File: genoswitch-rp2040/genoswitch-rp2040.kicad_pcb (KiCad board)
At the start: 2 copper layers, 43.4 x 57.3 mm, 42 parts, among them J1 USB_B_Micro, J10 RP2040_ADC2, J11 RP2040_ADC3, J2 Conn_01x03_Socket-PicoDebug, J3 HW-SPI0, J4 HW-SPI1, J5 PIO-SPI0, J6 PIO-SPI1, J7 SERIAL, J8 RP2040_ADC0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

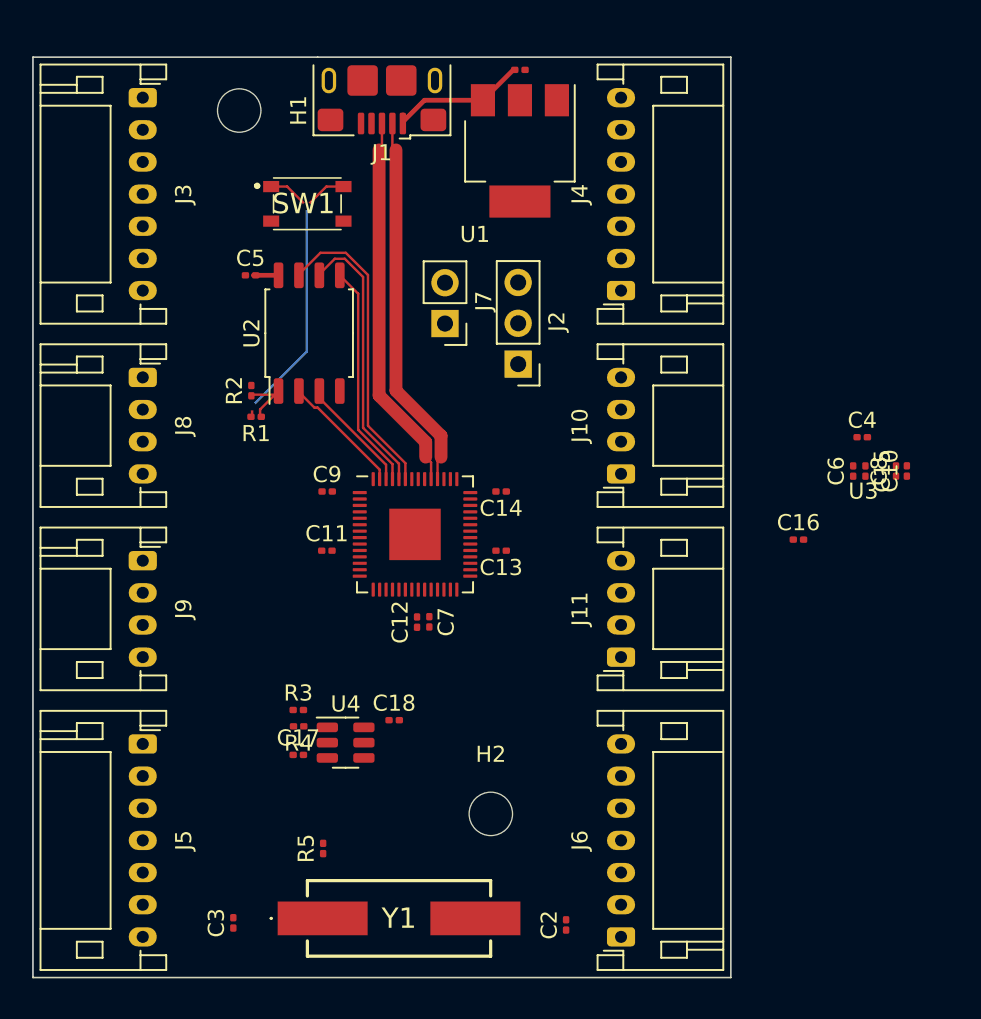
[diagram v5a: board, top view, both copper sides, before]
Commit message: Initial routing of C6, C15, C16, R6, R7
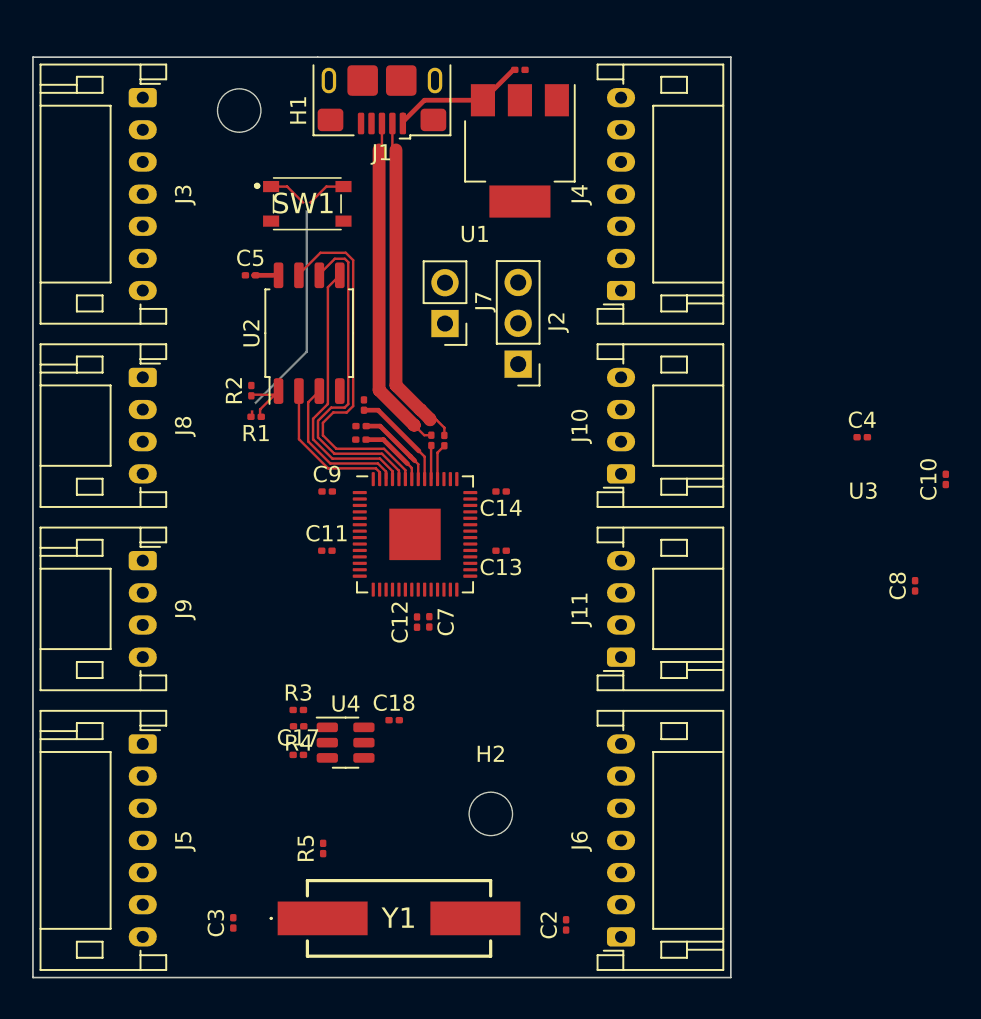
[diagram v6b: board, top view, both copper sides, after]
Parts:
- added R6: 27.4, Resistor_SMD:R_0201_0603Metric, F.Cu at (110.4, 68.1)
- added R7: 27.4, Resistor_SMD:R_0201_0603Metric, F.Cu at (111.2, 68.1)
- moved C15 31.5 mm to (106.0, 67.2), turned to 0 degrees
- moved C6 30.7 mm to (106.0, 68.0), turned to 180 degrees
- moved C16 28.3 mm to (106.2, 65.9), turned to -90 degrees
- moved C8 7.24 mm to (140.5, 77.1)
- moved C10 2.48 mm to (142.4, 70.5)
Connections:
- U3 pad 46: /USB_D- -> Net-(U3-USB_DM)
- U3 pad 47: /USB_D+ -> Net-(U3-USB_DP)
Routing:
- net GND: track 0.00 -> 11.5 mm
- net +1V1: track 0.00 -> 4.27 mm
- net /QSPI_SD3: track 19.1 -> 22.9 mm
- net /QSPI_SCLK: track 17.1 -> 20.9 mm
- net /QSPI_SD0: track 14.1 -> 17.2 mm
- net /USB_D-: track 23.5 -> 21.0 mm
- net /USB_D+: track 23.5 -> 21.1 mm
- net /QSPI_SD2: track 7.20 -> 9.51 mm
- net Net-(U3-USB_DM): track 0.00 -> 2.25 mm
- net Net-(U3-USB_DP): track 0.00 -> 2.10 mm
- net /QSPI_SD1: track 7.67 -> 9.30 mm

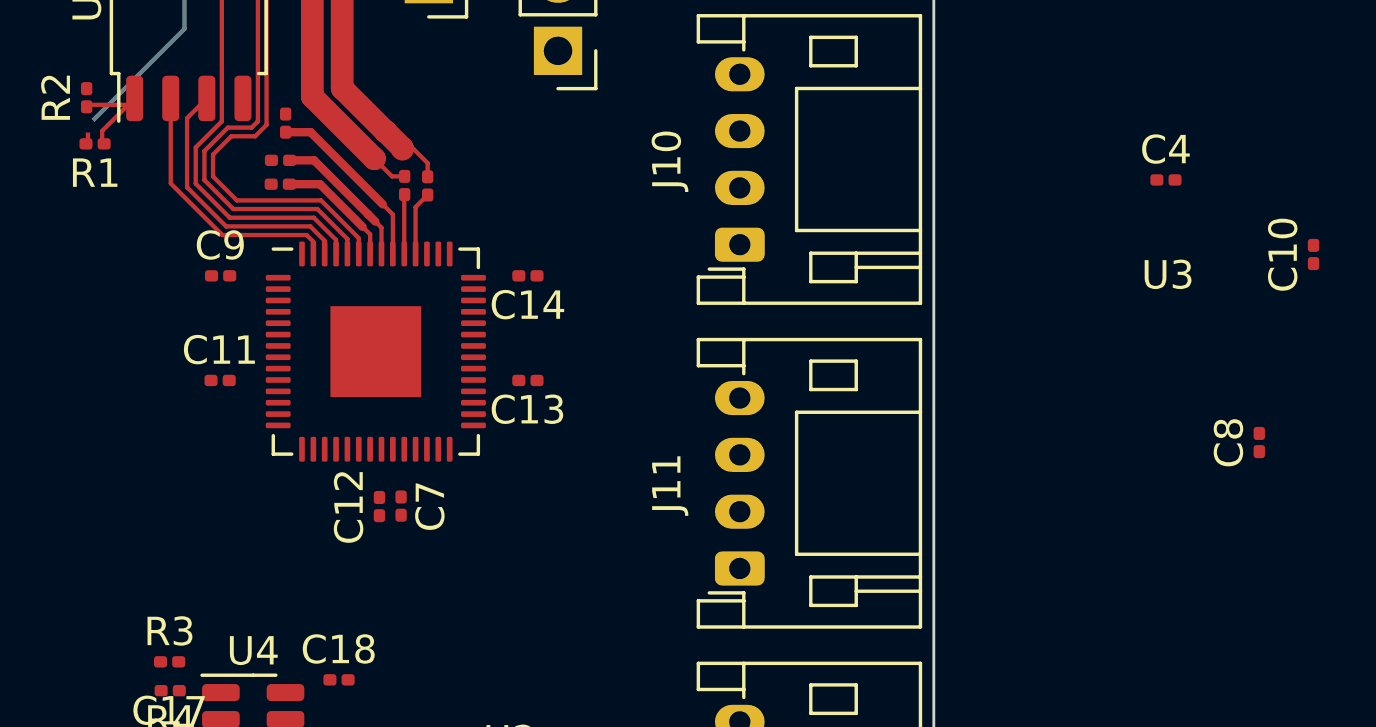
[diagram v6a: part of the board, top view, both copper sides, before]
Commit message: Route other resistors, caps on RP2040
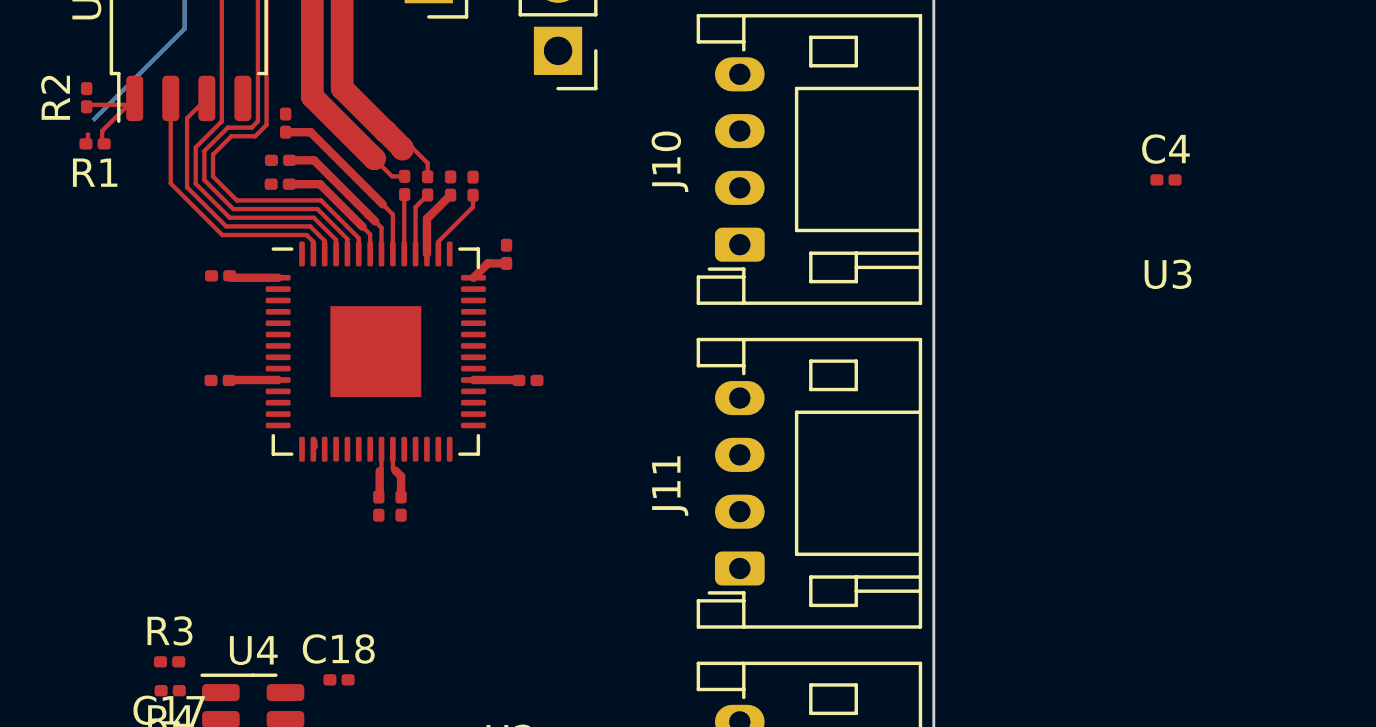
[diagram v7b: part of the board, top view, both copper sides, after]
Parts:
- moved C8 29.9 mm to (112.0, 68.1)
- moved C10 29.7 mm to (112.8, 68.1)
- moved C14 1.07 mm to (114.0, 70.5), turned to -90 degrees
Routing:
- net GND: track 11.5 -> 19.7 mm
- net +1V1: track 4.27 -> 8.49 mm
- net Net-(U3-VREG_IN): track 0.00 -> 2.58 mm
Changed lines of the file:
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@@
   (setup
     (pad_to_mask_clearance 0)
-    (grid_origin 108.712 0)
     (pcbplotparams
       (layerselection 0x00010fc_ffffffff)
@@
   )
   (footprint "Capacitor_SMD:C_0201_0603Metric" (layer "F.Cu")
-    (at 142.362 70.495 90)
+    (at 112.77 68.09 90)
     (descr "Capacitor SMD 0201 (0603 Metric), square (rectangular) end terminal, IPC_7351 nominal, (Body size source: https://www.vishay.com/docs/20052/crcw0201e3.pdf), generated with kicad-footprint-generator")
     (tags "capacitor")
@@
     (property "ki_keywords" "cap capacitor")
     (attr smd)
-    (fp_text reference "C10" (at 0 -1.05 90) (layer "F.SilkS")
+    (fp_text reference "C10" (at 0 -1.05 90) (layer "F.SilkS") hide
         (effects (font (size 1 1) (thickness 0.15)))
     )
@@
   )
   (footprint "Capacitor_SMD:C_0201_0603Metric" (layer "F.Cu")
-    (at 114.702 71.247 180)
+    (at 113.95 70.49 -90)
     (descr "Capacitor SMD 0201 (0603 Metric), square (rectangular) end terminal, IPC_7351 nominal, (Body size source: https://www.vishay.com/docs/20052/crcw0201e3.pdf), generated with kicad-footprint-generator")
     (tags "capacitor")
@@
     (property "ki_keywords" "cap capacitor")
     (attr smd)
-    (fp_text reference "C14" (at 0 -1.05 180) (layer "F.SilkS")
+    (fp_text reference "C14" (at 0 -1.05 90) (layer "F.SilkS") hide
         (effects (font (size 1 1) (thickness 0.15)))
     )
-    (fp_text value "100nF" (at 0 1.05 180) (layer "F.Fab")
+    (fp_text value "100nF" (at 0 1.05 90) (layer "F.Fab")
         (effects (font (size 1 1) (thickness 0.15)))
     )
-    (fp_text user "${REFERENCE}" (at 0 -0.68 180) (layer "F.Fab")
+    (fp_text user "${REFERENCE}" (at 0 -0.68 90) (layer "F.Fab")
         (effects (font (size 0.25 0.25) (thickness 0.04)))
     )
@@
     (fp_line (start 0.3 0.15) (end -0.3 0.15)
       (stroke (width 0.1) (type solid)) (layer "F.Fab"))
-    (pad "" smd roundrect (at -0.345 0 180) (size 0.318 0.36) (layers "F.Paste") (roundrect_rratio 0.25))
-    (pad "" smd roundrect (at 0.345 0 180) (size 0.318 0.36) (layers "F.Paste") (roundrect_rratio 0.25))
-    (pad "1" smd roundrect (at -0.32 0 180) (size 0.46 0.4) (layers "F.Cu" "F.Mask") (roundrect_rratio 0.25)
+    (pad "" smd roundrect (at -0.345 0 270) (size 0.318 0.36) (layers "F.Paste") (roundrect_rratio 0.25))
+    (pad "" smd roundrect (at 0.345 0 270) (size 0.318 0.36) (layers "F.Paste") (roundrect_rratio 0.25))
+    (pad "1" smd roundrect (at -0.32 0 270) (size 0.46 0.4) (layers "F.Cu" "F.Mask") (roundrect_rratio 0.25)
       (net 5 "+3V3") (pintype "passive"))
-    (pad "2" smd roundrect (at 0.32 0 180) (size 0.46 0.4) (layers "F.Cu" "F.Mask") (roundrect_rratio 0.25)
+    (pad "2" smd roundrect (at 0.32 0 270) (size 0.46 0.4) (layers "F.Cu" "F.Mask") (roundrect_rratio 0.25)
       (net 2 "GND") (pintype "passive"))
     (model "${KICAD6_3DMODEL_DIR}/Capacitor_SMD.3dshapes/C_0201_0603Metric.wrl"
@@
     (property "ki_keywords" "cap capacitor")
     (attr smd)
-    (fp_text reference "C9" (at 0 -1.05) (layer "F.SilkS")
+    (fp_text reference "C9" (at 0 -1.05) (layer "F.SilkS") hide
         (effects (font (size 1 1) (thickness 0.15)))
     )
@@
   )
   (footprint "Capacitor_SMD:C_0201_0603Metric" (layer "F.Cu")
-    (at 140.452 77.115 90)
+    (at 111.98 68.085 90)
     (descr "Capacitor SMD 0201 (0603 Metric), square (rectangular) end terminal, IPC_7351 nominal, (Body size source: https://www.vishay.com/docs/20052/crcw0201e3.pdf), generated with kicad-footprint-generator")
     (tags "capacitor")
@@
     (property "ki_keywords" "cap capacitor")
     (attr smd)
-    (fp_text reference "C8" (at 0 -1.05 90) (layer "F.SilkS")
+    (fp_text reference "C8" (at 0 -1.05 90) (layer "F.SilkS") hide
         (effects (font (size 1 1) (thickness 0.15)))
     )
@@
     (property "ki_keywords" "cap capacitor")
     (attr smd)
-    (fp_text reference "C11" (at 0 -1.05) (layer "F.SilkS")
+    (fp_text reference "C11" (at 0 -1.05) (layer "F.SilkS") hide
         (effects (font (size 1 1) (thickness 0.15)))
     )
@@
     (property "ki_keywords" "cap capacitor")
     (attr smd)
-    (fp_text reference "C13" (at 0 -1.05 180) (layer "F.SilkS")
+    (fp_text reference "C13" (at 0 -1.05 180) (layer "F.SilkS") hide
         (effects (font (size 1 1) (thickness 0.15)))
     )
@@
   )
   (footprint "Capacitor_SMD:C_0201_0603Metric" (layer "F.Cu")
-    (at 109.474 79.371 90)
+    (at 109.452 79.355 90)
     (descr "Capacitor SMD 0201 (0603 Metric), square (rectangular) end terminal, IPC_7351 nominal, (Body size source: https://www.vishay.com/docs/20052/crcw0201e3.pdf), generated with kicad-footprint-generator")
     (tags "capacitor")
@@
     (property "ki_keywords" "cap capacitor")
     (attr smd)
-    (fp_text reference "C12" (at 0 -1.05 90) (layer "F.SilkS")
+    (fp_text reference "C12" (at 0 -1.05 90) (layer "F.SilkS") hide
         (effects (font (size 1 1) (thickness 0.15)))
     )
@@
     (property "ki_keywords" "cap capacitor")
     (attr smd)
-    (fp_text reference "C7" (at 0 -1.05 -90) (layer "F.SilkS")
+    (fp_text reference "C7" (at 0 -1.05 90) (layer "F.SilkS") hide
         (effects (font (size 1 1) (thickness 0.15)))
     )
-    (fp_text value "100nF" (at 0 1.05 -90) (layer "F.Fab")
+    (fp_text value "100nF" (at 0 1.05 90) (layer "F.Fab")
         (effects (font (size 1 1) (thickness 0.15)))
     )
-    (fp_text user "${REFERENCE}" (at 0 -0.68 -90) (layer "F.Fab")
+    (fp_text user "${REFERENCE}" (at 0 -0.68 90) (layer "F.Fab")
         (effects (font (size 0.25 0.25) (thickness 0.04)))
     )
@@
   (segment (start 115.622 45.02) (end 115.462 45.02) (width 0.295656) (layer "F.Cu") (net 1))
   (segment (start 108.59 48.25486) (end 108.59 48.358) (width 0.295656) (layer "F.Cu") (net 1))
+  (segment (start 109.547 78.055) (end 109.482 78.12) (width 0.1524) (layer "F.Cu") (net 2))
   (segment (start 109.078823 69.083177) (end 109.330056 69.33441) (width 0.295656) (layer "F.Cu") (net 2))
   (segment (start 109.547 69.551354) (end 109.330056 69.33441) (width 0.1524) (layer "F.Cu") (net 2))
@@
   (segment (start 106.172 66.19) (end 107.052 66.19) (width 0.295656) (layer "F.Cu") (net 2))
   (segment (start 109.547 70.4765) (end 109.547 69.551354) (width 0.1524) (layer "F.Cu") (net 2))
+  (segment (start 109.482 79.005) (end 109.452 79.035) (width 0.295656) (layer "F.Cu") (net 2))
+  (segment (start 105.9095 74.914) (end 104.201 74.914) (width 0.295656) (layer "F.Cu") (net 2))
   (segment (start 107.175646 67.18) (end 109.078823 69.083177) (width 0.295656) (layer "F.Cu") (net 2))
+  (segment (start 104.269 71.314) (end 104.202 71.247) (width 0.295656) (layer "F.Cu") (net 2))
+  (segment (start 109.547 77.3515) (end 109.547 78.055) (width 0.1524) (layer "F.Cu") (net 2))
+  (segment (start 105.9095 71.314) (end 104.269 71.314) (width 0.295656) (layer "F.Cu") (net 2))
   (segment (start 106.312 67.18) (end 107.175646 67.18) (width 0.295656) (layer "F.Cu") (net 2))
+  (segment (start 109.482 78.12) (end 109.482 79.005) (width 0.295656) (layer "F.Cu") (net 2))
+  (segment (start 104.201 74.914) (end 104.185 74.93) (width 0.295656) (layer "F.Cu") (net 2))
   (segment (start 109.947 69.085) (end 109.592 68.73) (width 0.1524) (layer "F.Cu") (net 2))
+  (segment (start 113.2885 70.81) (end 112.7845 71.314) (width 0.295656) (layer "F.Cu") (net 2))
+  (segment (start 113.95 70.81) (end 113.2885 70.81) (width 0.295656) (layer "F.Cu") (net 2))
+  (segment (start 112.7845 74.914) (end 114.366 74.914) (width 0.295656) (layer "F.Cu") (net 2))
+  (segment (start 114.366 74.914) (end 114.382 74.93) (width 0.295656) (layer "F.Cu") (net 2))
   (segment (start 109.947 70.4765) (end 109.947 69.085) (width 0.1524) (layer "F.Cu") (net 2))
   (segment (start 100.857 57.8) (end 99.287 57.8) (width 0.295656) (layer "F.Cu") (net 5))
   (segment (start 107.382 68.02) (end 108.882 69.52) (width 0.295656) (layer "F.Cu") (net 6))
+  (segment (start 110.236 78.304) (end 110.032 78.1) (width 0.295656) (layer "F.Cu") (net 6))
+  (segment (start 110.236 79.034) (end 110.236 78.304) (width 0.295656) (layer "F.Cu") (net 6))
+  (segment (start 109.947 77.3515) (end 109.947 78.015) (width 0.1524) (layer "F.Cu") (net 6))
+  (segment (start 111.147 69.238) (end 111.98 68.405) (width 0.295656) (layer "F.Cu") (net 6))
   (segment (start 109.147 69.785) (end 108.882 69.52) (width 0.1524) (layer "F.Cu") (net 6))
   (segment (start 109.147 70.4765) (end 109.147 69.785) (width 0.1524) (layer "F.Cu") (net 6))
   (segment (start 106.302 68.02) (end 107.382 68.02) (width 0.295656) (layer "F.Cu") (net 6))
+  (segment (start 109.947 78.015) (end 110.032 78.1) (width 0.1524) (layer "F.Cu") (net 6))
+  (segment (start 111.147 70.4765) (end 111.147 69.238) (width 0.295656) (layer "F.Cu") (net 6))
+  (segment (start 111.547 70.045) (end 112.77 68.822) (width 0.1524) (layer "F.Cu") (net 7))
+  (segment (start 111.547 70.4765) (end 111.547 70.045) (width 0.1524) (layer "F.Cu") (net 7))
+  (segment (start 112.77 68.822) (end 112.77 68.41) (width 0.1524) (layer "F.Cu") (net 7))
   (segment (start 111.544 70.4735) (end 111.547 70.4765) (width 0.15) (layer "F.Cu") (net 7))
   (segment (start 108.162 64.643104) (end 109.686496 66.1676) (width 0.8) (layer "F.Cu") (net 10))
@@
   (segment (start 107.29 48.358) (end 107.29 49.822) (width 0.1524) (layer "F.Cu") (net 11))
   (segment (start 107.29 49.822) (end 107.112 50) (width 0.1524) (layer "F.Cu") (net 11))
+  (segment (start 107.2184 77.2801) (end 107.2184 77.06) (width 0.1524) (layer "F.Cu") (net 27))
+  (segment (start 107.147 77.3515) (end 107.2184 77.2801) (width 0.1524) (layer "F.Cu") (net 27))
   (segment (start 100.857 65) (end 99.712 66.145) (width 0.1524) (layer "F.Cu") (net 34))
   (segment (start 100.632 65.225) (end 100.857 65) (width 0.1524) (layer "F.Cu") (net 34))
